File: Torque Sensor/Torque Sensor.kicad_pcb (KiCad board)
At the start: 2 copper layers, 5 parts, among them U2 MCP3561R, U4 AP2112K-3.3 (REG LINEAR 3.3V)

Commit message: updated nets
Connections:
- U2 pad 13: unconnected-(U2-~{CS}-Pad13) -> Net-(U2-~{CS})
- U2 pad 14: unconnected-(U2-SCLK-Pad14) -> Net-(U2-SCLK)
- U2 pad 15: unconnected-(U2-SDI-Pad15) -> Net-(U2-SDI)
- U2 pad 16: unconnected-(U2-SDO-Pad16) -> Net-(U2-SDO)
- U2 pad 17: unconnected-(U2-IRQ/MDAT-Pad17) -> Net-(U2-IRQ/MDAT)
- U2 pad 2: unconnected-(U2-AV_{GND}-Pad2) -> GND
- U2 pad 20: +3.3V -> Net-(U2-DV_{DD})
- U2 pad 3: unconnected-(U2-REFIN--Pad3) -> GND
- U2 pad 4: unconnected-(U2-REF_{IN+/OUT}-Pad4) -> Net-(J1-Pin_1)
- U2 pad 5: unconnected-(U2-CH0-Pad5) -> Net-(U2-CH0)
- U2 pad 6: unconnected-(U2-CH1-Pad6) -> Net-(U2-CH1)
- U6 pad 1: unconnected-(U6-A0-Pad1) -> ADC CS
- U6 pad 10: unconnected-(U6-MISO-Pad10) -> ADC SDO
- U6 pad 12: unconnected-(U6-SCK-Pad12) -> ADC SCLK
- U6 pad 3: unconnected-(U6-A1-Pad3) -> ADC IRQ
- U6 pad 8: unconnected-(U6-MOSI-Pad8) -> ADC SDI
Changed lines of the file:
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@@
 	)
 	(net 0 "")
-	(net 1 "unconnected-(U2-REF_{IN+{slash}OUT}-Pad4)")
-	(net 2 "unconnected-(U2-~{CS}-Pad13)")
-	(net 3 "unconnected-(U2-SCLK-Pad14)")
-	(net 4 "unconnected-(U2-MCLK-Pad18)")
-	(net 5 "unconnected-(U2-CH0-Pad5)")
-	(net 6 "unconnected-(U2-REFIN--Pad3)")
-	(net 7 "unconnected-(U2-IRQ{slash}MDAT-Pad17)")
-	(net 8 "unconnected-(U2-SDO-Pad16)")
-	(net 9 "unconnected-(U2-CH1-Pad6)")
-	(net 10 "unconnected-(U2-SDI-Pad15)")
-	(net 11 "+BATT")
-	(net 12 "Net-(D1-K)")
-	(net 13 "GND")
-	(net 14 "+3.3VA")
-	(net 15 "+3.3V")
-	(net 16 "unconnected-(U4-NC-Pad4)")
-	(net 17 "unconnected-(U6-SCK-Pad12)")
-	(net 18 "unconnected-(U6-MISO-Pad10)")
-	(net 19 "unconnected-(U6-A2-Pad5)")
-	(net 20 "unconnected-(U6-RX-Pad14)")
-	(net 21 "unconnected-(U6-A3-Pad7)")
-	(net 22 "unconnected-(U6-SCL-Pad11)")
-	(net 23 "unconnected-(U6-TX-Pad13)")
-	(net 24 "unconnected-(U6-MOSI-Pad8)")
-	(net 25 "unconnected-(U6-A0-Pad1)")
-	(net 26 "unconnected-(U6-A1-Pad3)")
-	(net 27 "unconnected-(U6-SDA-Pad9)")
-	(net 28 "Net-(U2-AV_{DD})")
-	(net 29 "unconnected-(U2-AV_{GND}-Pad2)")
+	(net 1 "unconnected-(U2-MCLK-Pad18)")
+	(net 2 "+BATT")
+	(net 3 "Net-(D1-K)")
+	(net 4 "GND")
+	(net 5 "+3.3VA")
+	(net 6 "+3.3V")
+	(net 7 "unconnected-(U4-NC-Pad4)")
+	(net 8 "unconnected-(U6-A2-Pad5)")
+	(net 9 "unconnected-(U6-RX-Pad14)")
+	(net 10 "unconnected-(U6-A3-Pad7)")
+	(net 11 "unconnected-(U6-SCL-Pad11)")
+	(net 12 "unconnected-(U6-TX-Pad13)")
+	(net 13 "unconnected-(U6-SDA-Pad9)")
+	(net 14 "Net-(U2-AV_{DD})")
+	(net 15 "Net-(J1-Pin_1)")
+	(net 16 "Net-(U2-~{CS})")
+	(net 17 "Net-(U2-SCLK)")
+	(net 18 "Net-(U2-CH0)")
+	(net 19 "Net-(U2-IRQ{slash}MDAT)")
+	(net 20 "Net-(U2-DV_{DD})")
+	(net 21 "Net-(U2-SDO)")
+	(net 22 "Net-(U2-CH1)")
+	(net 23 "Net-(U2-SDI)")
+	(net 24 "ADC SCLK")
+	(net 25 "ADC SDO")
+	(net 26 "ADC SDI")
+	(net 27 "ADC CS")
+	(net 28 "ADC IRQ")
 	(footprint "Diode_SMD:D_SOD-123"
 		(layer "F.Cu")
@@
 			(layers "F.Cu" "F.Mask" "F.Paste")
 			(roundrect_rratio 0.25)
-			(net 12 "Net-(D1-K)")
+			(net 3 "Net-(D1-K)")
 			(pinfunction "K")
 			(pintype "passive")
@@
 			(layers "F.Cu" "F.Mask" "F.Paste")
 			(roundrect_rratio 0.25)
-			(net 11 "+BATT")
+			(net 2 "+BATT")
 			(pinfunction "A")
 			(pintype "passive")
@@
 			(layers "*.Cu" "*.Mask")
 			(remove_unused_layers no)
-			(net 11 "+BATT")
+			(net 2 "+BATT")
 			(pinfunction "+")
 			(pintype "passive")
@@
 			(layers "*.Cu" "*.Mask")
 			(remove_unused_layers no)
-			(net 13 "GND")
+			(net 4 "GND")
 			(pinfunction "-")
 			(pintype "passive")
@@
 			(layers "F.Cu" "F.Mask" "F.Paste")
 			(roundrect_rratio 0.25)
-			(net 11 "+BATT")
+			(net 2 "+BATT")
 			(pinfunction "VIN")
 			(pintype "power_in")
@@
 			(layers "F.Cu" "F.Mask" "F.Paste")
 			(roundrect_rratio 0.25)
-			(net 13 "GND")
+			(net 4 "GND")
 			(pinfunction "GND")
 			(pintype "power_in")
@@
 			(layers "F.Cu" "F.Mask" "F.Paste")
 			(roundrect_rratio 0.25)
-			(net 11 "+BATT")
+			(net 2 "+BATT")
 			(pinfunction "EN")
 			(pintype "input")
@@
 			(layers "F.Cu" "F.Mask" "F.Paste")
 			(roundrect_rratio 0.25)
-			(net 16 "unconnected-(U4-NC-Pad4)")
+			(net 7 "unconnected-(U4-NC-Pad4)")
 			(pinfunction "NC")
 			(pintype "no_connect")
@@
 			(layers "F.Cu" "F.Mask" "F.Paste")
 			(roundrect_rratio 0.25)
-			(net 14 "+3.3VA")
+			(net 5 "+3.3VA")
 			(pinfunction "VOUT")
 			(pintype "power_out")
@@
 			(layers "F.Cu" "F.Mask" "F.Paste")
 			(roundrect_rratio 0.25)
-			(net 28 "Net-(U2-AV_{DD})")
+			(net 14 "Net-(U2-AV_{DD})")
 			(pinfunction "AV_{DD}")
 			(pintype "power_in")
@@
 			(layers "F.Cu" "F.Mask" "F.Paste")
 			(roundrect_rratio 0.25)
-			(net 29 "unconnected-(U2-AV_{GND}-Pad2)")
+			(net 4 "GND")
 			(pinfunction "AV_{GND}")
 			(pintype "power_in")
@@
 			(layers "F.Cu" "F.Mask" "F.Paste")
 			(roundrect_rratio 0.25)
-			(net 6 "unconnected-(U2-REFIN--Pad3)")
+			(net 4 "GND")
 			(pinfunction "REFIN-")
 			(pintype "power_in")
@@
 			(layers "F.Cu" "F.Mask" "F.Paste")
 			(roundrect_rratio 0.25)
-			(net 1 "unconnected-(U2-REF_{IN+{slash}OUT}-Pad4)")
+			(net 15 "Net-(J1-Pin_1)")
 			(pinfunction "REF_{IN+/OUT}")
 			(pintype "power_in")
@@
 			(layers "F.Cu" "F.Mask" "F.Paste")
 			(roundrect_rratio 0.25)
-			(net 5 "unconnected-(U2-CH0-Pad5)")
+			(net 18 "Net-(U2-CH0)")
 			(pinfunction "CH0")
 			(pintype "input")
@@
 			(layers "F.Cu" "F.Mask" "F.Paste")
 			(roundrect_rratio 0.25)
-			(net 9 "unconnected-(U2-CH1-Pad6)")
+			(net 22 "Net-(U2-CH1)")
 			(pinfunction "CH1")
 			(pintype "input")
@@
 			(layers "F.Cu" "F.Mask" "F.Paste")
 			(roundrect_rratio 0.25)
-			(net 2 "unconnected-(U2-~{CS}-Pad13)")
+			(net 16 "Net-(U2-~{CS})")
 			(pinfunction "~{CS}")
 			(pintype "input")
@@
 			(layers "F.Cu" "F.Mask" "F.Paste")
 			(roundrect_rratio 0.25)
-			(net 3 "unconnected-(U2-SCLK-Pad14)")
+			(net 17 "Net-(U2-SCLK)")
 			(pinfunction "SCLK")
 			(pintype "input")
@@
 			(layers "F.Cu" "F.Mask" "F.Paste")
 			(roundrect_rratio 0.25)
-			(net 10 "unconnected-(U2-SDI-Pad15)")
+			(net 23 "Net-(U2-SDI)")
 			(pinfunction "SDI")
 			(pintype "input")
@@
 			(layers "F.Cu" "F.Mask" "F.Paste")
 			(roundrect_rratio 0.25)
-			(net 8 "unconnected-(U2-SDO-Pad16)")
+			(net 21 "Net-(U2-SDO)")
 			(pinfunction "SDO")
 			(pintype "output")
@@
 			(layers "F.Cu" "F.Mask" "F.Paste")
 			(roundrect_rratio 0.25)
-			(net 7 "unconnected-(U2-IRQ{slash}MDAT-Pad17)")
+			(net 19 "Net-(U2-IRQ{slash}MDAT)")
 			(pinfunction "IRQ/MDAT")
 			(pintype "input")
@@
 			(layers "F.Cu" "F.Mask" "F.Paste")
 			(roundrect_rratio 0.25)
-			(net 4 "unconnected-(U2-MCLK-Pad18)")
+			(net 1 "unconnected-(U2-MCLK-Pad18)")
 			(pinfunction "MCLK")
 			(pintype "input")
@@
 			(layers "F.Cu" "F.Mask" "F.Paste")
 			(roundrect_rratio 0.25)
-			(net 13 "GND")
+			(net 4 "GND")
 			(pinfunction "VD_{GND}")
 			(pintype "power_in")
@@
 			(layers "F.Cu" "F.Mask" "F.Paste")
 			(roundrect_rratio 0.25)
-			(net 15 "+3.3V")
+			(net 20 "Net-(U2-DV_{DD})")
 			(pinfunction "DV_{DD}")
 			(pintype "power_in")
@@
 			(size 3.44 2)
 			(layers "F.Cu" "F.Mask" "B.SilkS" "F.Paste")
-			(net 25 "unconnected-(U6-A0-Pad1)")
+			(net 27 "ADC CS")
 			(pinfunction "A0")
 			(pintype "bidirectional")
@@
 			(size 3.44 2)
 			(layers "F.Cu" "F.Mask" "F.Paste")
-			(net 12 "Net-(D1-K)")
+			(net 3 "Net-(D1-K)")
 			(pinfunction "5V")
 			(pintype "input")
@@
 			(size 3.44 2)
 			(layers "F.Cu" "F.Mask" "F.Paste")
-			(net 26 "unconnected-(U6-A1-Pad3)")
+			(net 28 "ADC IRQ")
 			(pinfunction "A1")
 			(pintype "bidirectional")
@@
 			(size 3.44 2)
 			(layers "F.Cu" "F.Mask" "F.Paste")
-			(net 13 "GND")
+			(net 4 "GND")
 			(pinfunction "GND")
 			(pintype "input")
@@
 			(size 3.44 2)
 			(layers "F.Cu" "F.Mask" "F.Paste")
-			(net 19 "unconnected-(U6-A2-Pad5)")
+			(net 8 "unconnected-(U6-A2-Pad5)")
 			(pinfunction "A2")
 			(pintype "bidirectional")
@@
 			(size 3.44 2)
 			(layers "F.Cu" "F.Mask" "F.Paste")
-			(net 15 "+3.3V")
+			(net 6 "+3.3V")
 			(pinfunction "3.3V")
 			(pintype "output")
@@
 			(size 3.44 2)
 			(layers "F.Cu" "F.Mask" "F.Paste")
-			(net 21 "unconnected-(U6-A3-Pad7)")
+			(net 10 "unconnected-(U6-A3-Pad7)")
 			(pinfunction "A3")
 			(pintype "bidirectional")
@@
 			(size 3.44 2)
 			(layers "F.Cu" "F.Mask" "F.Paste")
-			(net 24 "unconnected-(U6-MOSI-Pad8)")
+			(net 26 "ADC SDI")
 			(pinfunction "MOSI")
 			(pintype "bidirectional")
@@
 			(size 3.44 2)
 			(layers "F.Cu" "F.Mask" "F.Paste")
-			(net 27 "unconnected-(U6-SDA-Pad9)")
+			(net 13 "unconnected-(U6-SDA-Pad9)")
 			(pinfunction "SDA")
 			(pintype "bidirectional")
@@
 			(size 3.44 2)
 			(layers "F.Cu" "F.Mask" "F.Paste")
-			(net 18 "unconnected-(U6-MISO-Pad10)")
+			(net 25 "ADC SDO")
 			(pinfunction "MISO")
 			(pintype "bidirectional")
@@
 			(size 3.44 2)
 			(layers "F.Cu" "F.Mask" "F.Paste")
-			(net 22 "unconnected-(U6-SCL-Pad11)")
+			(net 11 "unconnected-(U6-SCL-Pad11)")
 			(pinfunction "SCL")
 			(pintype "bidirectional")
@@
 			(size 3.44 2)
 			(layers "F.Cu" "F.Mask" "F.Paste")
-			(net 17 "unconnected-(U6-SCK-Pad12)")
+			(net 24 "ADC SCLK")
 			(pinfunction "SCK")
 			(pintype "bidirectional")
@@
 			(size 3.44 2)
 			(layers "F.Cu" "F.Mask" "F.Paste")
-			(net 23 "unconnected-(U6-TX-Pad13)")
+			(net 12 "unconnected-(U6-TX-Pad13)")
 			(pinfunction "TX")
 			(pintype "bidirectional")
@@
 			(size 3.44 2)
 			(layers "F.Cu" "F.Mask" "F.Paste")
-			(net 20 "unconnected-(U6-RX-Pad14)")
+			(net 9 "unconnected-(U6-RX-Pad14)")
 			(pinfunction "RX")
 			(pintype "bidirectional")

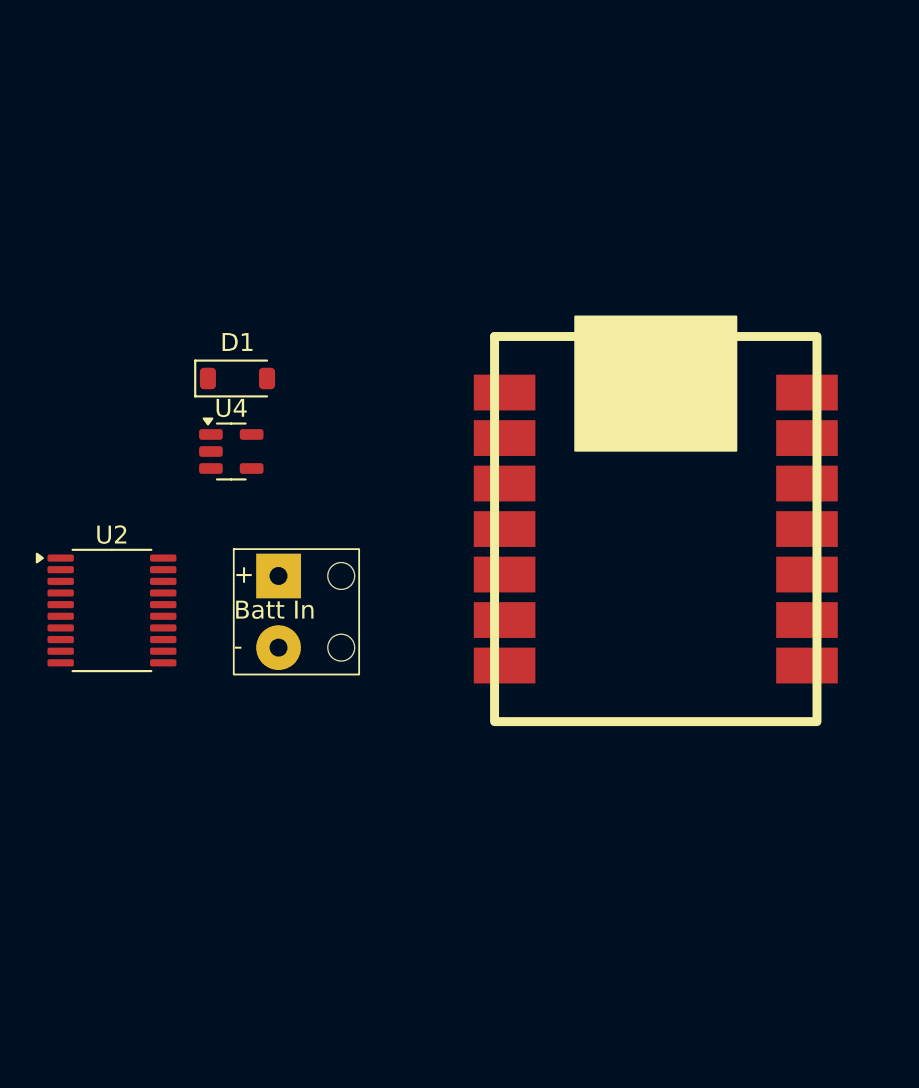
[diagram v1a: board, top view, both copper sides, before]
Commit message: Changed board to Feather rp2040 for charging circuitry, assigned footprints to caps and resistors.
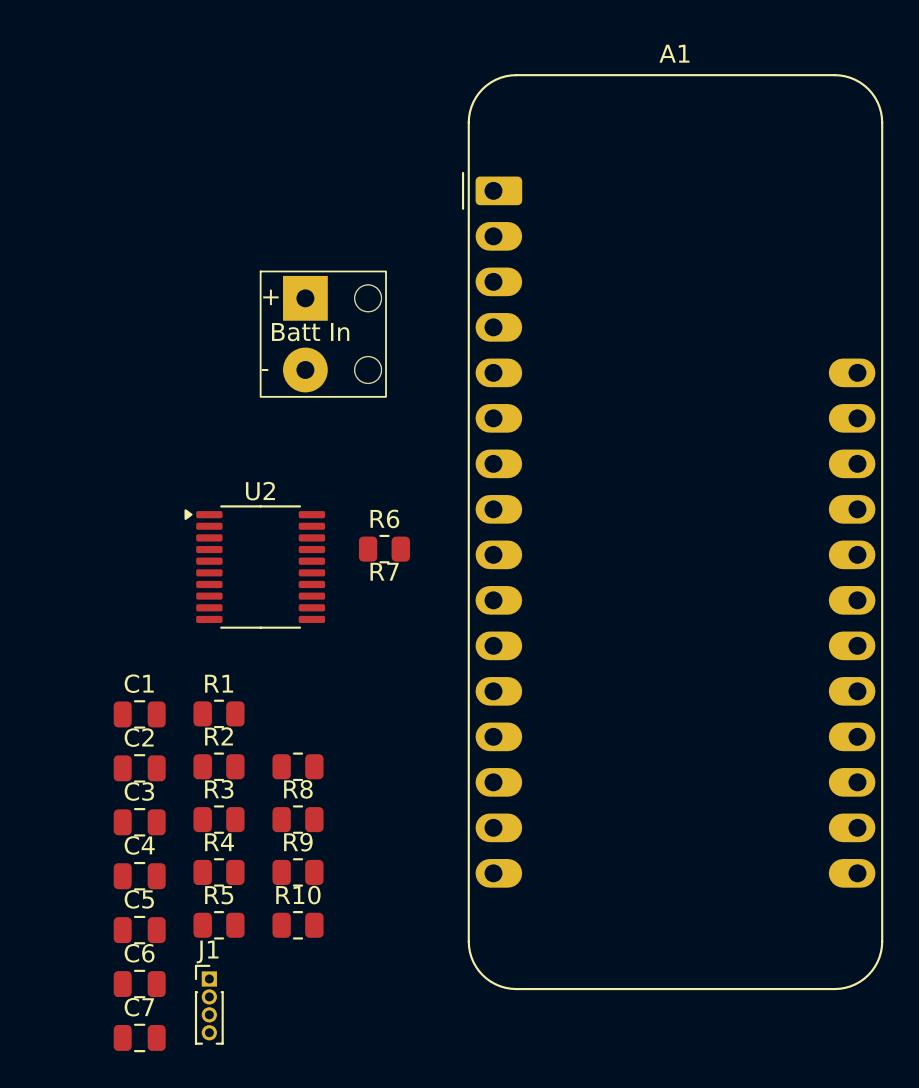
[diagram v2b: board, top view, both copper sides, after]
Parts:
- removed D1: MBR0520, Diode_SMD:D_SOD-123
- removed U4: AP2112K-3.3 (REG LINEAR 3.3V), Package_TO_SOT_SMD:SOT-23-5
- removed U6: ~, TestLib:Adafruit QT PY
- added A1: Adafruit_Feather_Generic, Module:Adafruit_Feather, F.Cu at (168.5, 70.0)
- added C1: 0.1uF 16V, Capacitor_SMD:C_0805_2012Metric, F.Cu at (148.7, 99.2)
- added C2: 0.1uF 16V, Capacitor_SMD:C_0805_2012Metric, F.Cu at (148.7, 102.2)
- added C3: 0.1uF 16V, Capacitor_SMD:C_0805_2012Metric, F.Cu at (148.7, 105.2)
- added C4: 0.1uF 16V, Capacitor_SMD:C_0805_2012Metric, F.Cu at (148.7, 108.3)
- added C5: 10uF 10V, Capacitor_SMD:C_0805_2012Metric, F.Cu at (148.7, 111.3)
- added C6: 0.1uF 16V, Capacitor_SMD:C_0805_2012Metric, F.Cu at (148.7, 114.3)
- added C7: 0.1uF 16V, Capacitor_SMD:C_0805_2012Metric, F.Cu at (148.7, 117.3)
- added J1: Full Bridge Strain Guage, Connector_PinHeader_1.00mm:PinHeader_1x04_P1.00mm_Vertical, F.Cu at (152.6, 114.0)
- added R1: 10R, Resistor_SMD:R_0805_2012Metric, F.Cu at (153.2, 99.2)
- added R10: 10R, Resistor_SMD:R_0805_2012Metric, F.Cu at (157.6, 111.0)
- added R2: 100, Resistor_SMD:R_0805_2012Metric, F.Cu at (153.2, 102.2)
- added R3: 10R, Resistor_SMD:R_0805_2012Metric, F.Cu at (153.2, 105.1)
- added R4: 10kR, Resistor_SMD:R_0805_2012Metric, F.Cu at (153.2, 108.0)
- added R5: 100, Resistor_SMD:R_0805_2012Metric, F.Cu at (153.2, 111.0)
- added R6: 10R, Resistor_SMD:R_0805_2012Metric, F.Cu at (162.4, 90.0)
- added R7: 10R, Resistor_SMD:R_0805_2012Metric, F.Cu at (157.6, 102.2)
- added R8: 10R, Resistor_SMD:R_0805_2012Metric, F.Cu at (157.6, 105.1)
- added R9: 10R, Resistor_SMD:R_0805_2012Metric, F.Cu at (157.6, 108.0)
- moved U1 15.6 mm to (158.0, 76.5)
- moved U2 8.65 mm to (155.5, 91.0)

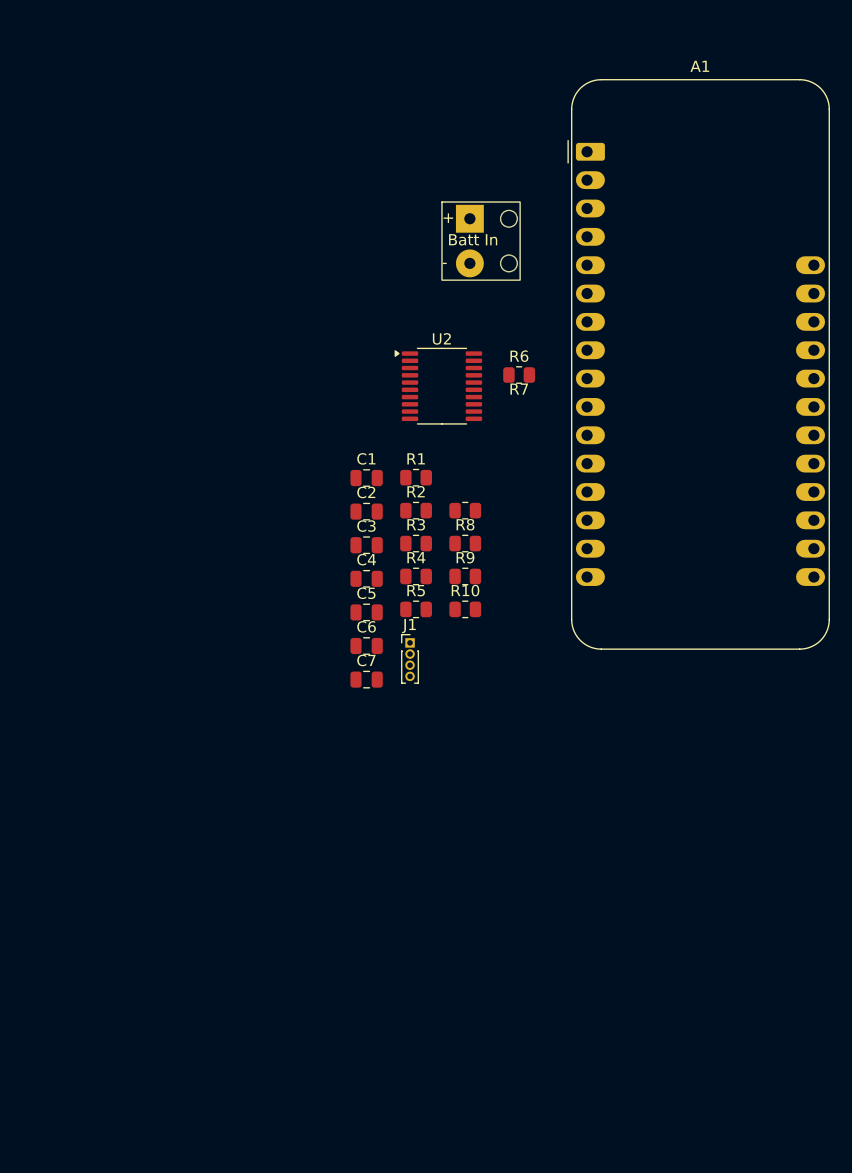
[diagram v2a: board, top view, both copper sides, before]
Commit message: Changed ADC to the more JLC stocked AD7173-8 (Rev. B)
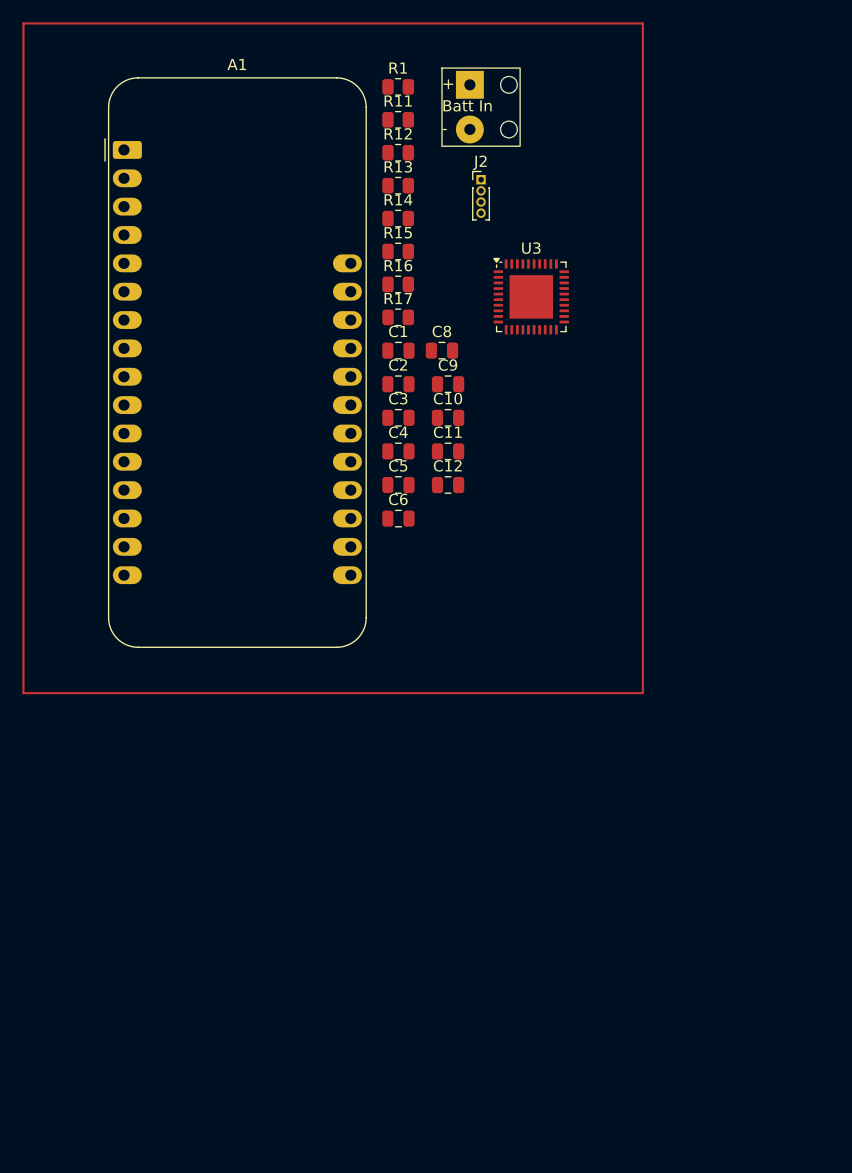
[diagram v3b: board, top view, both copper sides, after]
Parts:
- removed C7: 0.1uF 16V, Capacitor_SMD:C_0805_2012Metric
- removed J1: Full Bridge Strain Guage, Connector_PinHeader_1.00mm:PinHeader_1x04_P1.00mm_Vertical
- removed R10, R3, R6, R7, R8, R9: 10R, Resistor_SMD:R_0805_2012Metric
- removed R2, R5: 100, Resistor_SMD:R_0805_2012Metric
- removed R4: 10kR, Resistor_SMD:R_0805_2012Metric
- removed U2: MCP3561R, Package_SO:TSSOP-20_4.4x6.5mm_P0.65mm
- added C10: 0.1uF 16V, Capacitor_SMD:C_0805_2012Metric, F.Cu at (156.0, 93.8)
- added C11: .1uF 16V, Capacitor_SMD:C_0805_2012Metric, F.Cu at (156.0, 96.8)
- added C12: 0.1uF 16V, Capacitor_SMD:C_0805_2012Metric, F.Cu at (156.0, 99.9)
- added C8: 0.1uF 10V, Capacitor_SMD:C_0805_2012Metric, F.Cu at (155.5, 87.8)
- added C9: 0.1uF 16V, Capacitor_SMD:C_0805_2012Metric, F.Cu at (156.0, 90.8)
- added J2: Full Bridge Strain Guage, Connector_PinHeader_1.00mm:PinHeader_1x04_P1.00mm_Vertical, F.Cu at (159.0, 72.5)
- added R11: 10R, Resistor_SMD:R_0805_2012Metric, F.Cu at (151.6, 67.1)
- added R12: 10R, Resistor_SMD:R_0805_2012Metric, F.Cu at (151.6, 70.1)
- added R13: 10R, Resistor_SMD:R_0805_2012Metric, F.Cu at (151.6, 73.0)
- added R14: 10R, Resistor_SMD:R_0805_2012Metric, F.Cu at (151.6, 76.0)
- added R15: 100, Resistor_SMD:R_0805_2012Metric, F.Cu at (151.6, 78.9)
- added R16: 100, Resistor_SMD:R_0805_2012Metric, F.Cu at (151.6, 81.9)
- added R17: 10R, Resistor_SMD:R_0805_2012Metric, F.Cu at (151.6, 84.8)
- added U3: AD7173-8, Package_CSP:LFCSP-40-1EP_6x6mm_P0.5mm_EP3.9x3.9mm, F.Cu at (163.5, 83.0)
- C1, C3: value 0.1uF 16V -> .1uF 16V
- C4, C6: value 0.1uF 16V -> 1uF 16V
- C5: value 10uF 10V -> .1uF 16V
- moved A1 41.5 mm to (127.0, 69.8)
- moved R1 35.1 mm to (151.6, 64.2)
- moved U1 12.0 mm to (158.0, 64.5)
- moved C1 11.8 mm to (151.6, 87.8)
- moved C3 11.8 mm to (151.6, 93.8)
- moved C4 11.8 mm to (151.6, 96.8)
- moved C6 11.8 mm to (151.6, 102.9)
- moved C2 11.8 mm to (151.6, 90.8)
- moved C5 11.8 mm to (151.6, 99.9)
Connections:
- C1 pad 2: Net-(U2-AV_{DD}) -> AVDD
- C2 pad 2: Net-(U2-AV_{DD}) -> AVDD
- C5 pad 1: Net-(J1-Pin_1) -> GND
- C5 pad 2: GND -> Net-(U3-REGCAPA)
- C6 pad 2: Net-(U2-CH0) -> Net-(U3-REGCAPA)
- R1 pad 1: +3.3VA -> AVDD
- R1 pad 2: Net-(U2-AV_{DD}) -> +3.3V
